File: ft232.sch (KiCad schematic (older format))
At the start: 16 parts, among them J1 USB_B, U6 FT232RL, U7 4N25, U8 4N25

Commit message: Redesigned schematics and board
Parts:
- renumbered C36 to C39, C37 to C40, C38 to C41, D31 to D33, D32 to D34, R45 to R55, R46 to R56, R47 to R57, R48 to R58, R49 to R59, R50 to R60, R51 to R61, U6 to U7, U7 to U8, U8 to U9
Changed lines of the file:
@@
-EESchema Schematic File Version 2  date Thu 19 Jan 2012 12:17:41 AM EST
+EESchema Schematic File Version 2  date Fri 20 Jan 2012 02:23:37 PM EST
 LIBS:power
 LIBS:device
@@
 Sheet 7 7
 Title ""
-Date "19 jan 2012"
+Date "20 jan 2012"
 Rev ""
 Comp ""
@@
 Connection ~ 4250 3650
 $Comp
-L CP1 C37
+L CP1 C40
 U 1 1 4F179530
 P 4000 2000
-F 0 "C37" H 4050 2100 50  0000 L CNN
+F 0 "C40" H 4050 2100 50  0000 L CNN
 F 1 "4.7uF" H 4050 1900 50  0000 L CNN
 	1    4000 2000
@@
 5v-USB
 $Comp
-L R R45
+L R R55
 U 1 1 4F1794BF
 P 4500 3650
-F 0 "R45" V 4580 3650 50  0000 C CNN
+F 0 "R55" V 4580 3650 50  0000 C CNN
 F 1 "2k" V 4500 3650 50  0000 C CNN
 	1    4500 3650
@@
 $EndComp
 $Comp
-L R R51
+L R R61
 U 1 1 4F17944E
 P 10850 3000
-F 0 "R51" V 10930 3000 50  0000 C CNN
+F 0 "R61" V 10930 3000 50  0000 C CNN
 F 1 "2.4k" V 10850 3000 50  0000 C CNN
 	1    10850 3000
@@
 5v-USB
 $Comp
-L R R49
+L R R59
 U 1 1 4F1793A2
 P 9400 3100
-F 0 "R49" V 9480 3100 50  0000 C CNN
+F 0 "R59" V 9480 3100 50  0000 C CNN
 F 1 "10k" V 9400 3100 50  0000 C CNN
 	1    9400 3100
@@
 GND
 $Comp
-L R R50
+L R R60
 U 1 1 4F1792E7
 P 9600 2050
-F 0 "R50" V 9680 2050 50  0000 C CNN
+F 0 "R60" V 9680 2050 50  0000 C CNN
 F 1 "10k" V 9600 2050 50  0000 C CNN
 	1    9600 2050
@@
 NoConn ~ 9350 2200
 $Comp
-L R R46
+L R R56
 U 1 1 4F179239
 P 8100 1950
-F 0 "R46" V 8180 1950 50  0000 C CNN
+F 0 "R56" V 8180 1950 50  0000 C CNN
 F 1 "2.4k" V 8100 1950 50  0000 C CNN
 	1    8100 1950
@@
 5v-USB
 $Comp
-L OPTO-TRANSISTOR U8
+L OPTO-TRANSISTOR U9
 U 1 1 4F1790EA
 P 10200 3450
-F 0 "U8" H 10400 3750 60  0000 C CNN
+F 0 "U9" H 10400 3750 60  0000 C CNN
 F 1 "4N25" H 10300 3150 60  0000 C CNN
 	1    10200 3450
@@
 $EndComp
 $Comp
-L OPTO-TRANSISTOR U7
+L OPTO-TRANSISTOR U8
 U 1 1 4F1790E6
 P 8750 2400
-F 0 "U7" H 8950 2700 60  0000 C CNN
+F 0 "U8" H 8950 2700 60  0000 C CNN
 F 1 "4N25" H 8850 2100 60  0000 C CNN
 	1    8750 2400
@@
 USB-GND
 $Comp
-L C C36
+L C C39
 U 1 1 4F0A45B0
 P 3550 2000
-F 0 "C36" H 3600 2100 50  0000 L CNN
+F 0 "C39" H 3600 2100 50  0000 L CNN
 F 1 "0.1uF" H 3600 1900 50  0000 L CNN
 	1    3550 2000
@@
 NoConn ~ 2200 2650
 $Comp
-L R R48
+L R R58
 U 1 1 4F0A4640
 P 8150 3950
-F 0 "R48" V 8230 3950 50  0000 C CNN
+F 0 "R58" V 8230 3950 50  0000 C CNN
 F 1 "470" V 8150 3950 50  0000 C CNN
 	1    8150 3950
@@
 $EndComp
 $Comp
-L R R47
+L R R57
 U 1 1 4F0A462A
 P 8150 3650
-F 0 "R47" V 8230 3650 50  0000 C CNN
+F 0 "R57" V 8230 3650 50  0000 C CNN
 F 1 "470" V 8150 3650 50  0000 C CNN
 	1    8150 3650
@@
 $EndComp
 $Comp
-L LED D32
+L LED D34
 U 1 1 4F0A4611
 P 7700 3950
-F 0 "D32" H 7700 4050 50  0000 C CNN
+F 0 "D34" H 7700 4050 50  0000 C CNN
 F 1 "LED" H 7700 3850 50  0000 C CNN
 	1    7700 3950
@@
 $EndComp
 $Comp
-L LED D31
+L LED D33
 U 1 1 4F0A45FE
 P 7700 3650
-F 0 "D31" H 7700 3750 50  0000 C CNN
+F 0 "D33" H 7700 3750 50  0000 C CNN
 F 1 "LED" H 7700 3550 50  0000 C CNN
 	1    7700 3650
@@
 $EndComp
 $Comp
-L C C38
+L C C41
 U 1 1 4F0A4530
 P 4950 4350
-F 0 "C38" H 5000 4450 50  0000 L CNN
+F 0 "C41" H 5000 4450 50  0000 L CNN
 F 1 "0.1uF" H 5000 4250 50  0000 L CNN
 	1    4950 4350
@@
 NoConn ~ 6800 4150
 $Comp
-L FT232RL U6
+L FT232RL U7
 U 1 1 4F0A4204
 P 5900 3650
-F 0 "U6" H 6300 2700 60  0000 C CNN
+F 0 "U7" H 6300 2700 60  0000 C CNN
 F 1 "FT232RL" H 5900 4550 60  0000 C CNN
 	1    5900 3650

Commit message: Updated Schematics, created new PDF, completed board layout and routing
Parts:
- removed U8, U9: 4N25, symbol OPTO-TRANSISTOR
- added JP3, JP4: JUMPER, symbol JUMPER
- added U8, U9: PS2911-1-F3-A, symbol PS2911-1-F3-A
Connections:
- wire segments 28 -> 30
- no-connect marks 15 -> 11
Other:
- moved on the sheet: R60, R61
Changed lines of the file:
@@
-EESchema Schematic File Version 2  date Fri 20 Jan 2012 02:23:37 PM EST
+EESchema Schematic File Version 2  date Sun 22 Jan 2012 12:58:37 AM EST
 LIBS:power
 LIBS:device
@@
 Sheet 7 7
 Title ""
-Date "20 jan 2012"
+Date "22 jan 2012"
 Rev ""
 Comp ""
@@
 Comment4 ""
 $EndDescr
+Connection ~ 7250 3250
+Connection ~ 7850 3250
+Wire Wire Line
+	7850 3250 7850 3150
+Wire Wire Line
+	7850 3150 6800 3150
+Connection ~ 6800 3450
+Connection ~ 7400 3450
+Wire Wire Line
+	7400 3450 7400 3350
+Wire Wire Line
+	7400 3350 6800 3350
+Connection ~ 4250 3650
+Connection ~ 4750 3650
+Connection ~ 4950 3650
+Wire Wire Line
+	4750 3650 4950 3650
+Connection ~ 6800 3150
+Connection ~ 6800 3250
+Connection ~ 6800 3350
+Connection ~ 6800 3450
+Wire Wire Line
+	9400 2850 9650 2850
+Wire Wire Line
+	6800 2950 8100 2950
+Wire Wire Line
+	8100 2950 8100 2500
+Connection ~ 8100 1700
+Connection ~ 8100 2500
+Connection ~ 9400 2850
+Connection ~ 9400 3350
+Connection ~ 9600 3350
+Connection ~ 9600 3650
+Wire Wire Line
+	9600 3650 9350 3650
+Connection ~ 8100 2200
+Wire Wire Line
+	8400 3950 8400 3650
+Wire Wire Line
+	2550 3150 2550 1800
+Wire Wire Line
+	6200 4850 4950 4850
+Connection ~ 6800 2950
+Connection ~ 6800 3050
+Connection ~ 8400 3950
+Connection ~ 8400 3650
+Connection ~ 7900 3650
+Connection ~ 7900 3950
+Connection ~ 7500 3950
+Connection ~ 7500 3650
+Connection ~ 6800 3750
+Connection ~ 6800 3850
+Connection ~ 6200 4850
+Connection ~ 6050 4850
+Connection ~ 5900 4850
+Connection ~ 5750 4850
+Connection ~ 4950 4550
+Connection ~ 4950 4150
+Connection ~ 4950 3350
+Connection ~ 4950 3250
+Connection ~ 4950 3000
+Connection ~ 4950 2900
+Connection ~ 2550 3450
+Connection ~ 2550 3350
+Connection ~ 2550 3250
+Connection ~ 2550 3150
+Connection ~ 3550 2200
+Connection ~ 3550 1800
+Wire Wire Line
+	7500 3950 7500 3850
+Wire Wire Line
+	7500 3850 6800 3850
+Wire Wire Line
+	2550 3350 4950 3350
+Connection ~ 5600 4850
+Wire Wire Line
+	2550 4550 4950 4550
+Wire Wire Line
+	4950 3250 2550 3250
+Wire Wire Line
+	7500 3650 7500 3750
+Wire Wire Line
+	7500 3750 6800 3750
+Wire Wire Line
+	2550 4550 2550 3450
+Wire Wire Line
+	4950 4550 4950 4850
+Wire Wire Line
+	2550 1800 4950 1800
+Wire Wire Line
+	4950 1800 4950 3000
+Wire Wire Line
+	8100 1700 7850 1700
+Wire Wire Line
+	6800 3050 8850 3050
+Wire Wire Line
+	8850 3050 8850 3350
+Wire Wire Line
+	8850 3350 9600 3350
+Wire Wire Line
+	4250 3650 4000 3650
+Wire Wire Line
+	3550 2200 4000 2200
+Connection ~ 4000 2200
 Connection ~ 4000 1800
-NoConn ~ 10550 3650
-NoConn ~ 8400 2600
-Connection ~ 4000 2200
-Wire Wire Line
-	3550 2200 4000 2200
-Wire Wire Line
-	4250 3650 4000 3650
-Wire Wire Line
-	6800 3350 6800 3450
-Wire Wire Line
-	9600 3350 8850 3350
-Wire Wire Line
-	8850 3350 8850 3050
-Wire Wire Line
-	8850 3050 6800 3050
-Wire Wire Line
-	8100 1700 7850 1700
-Wire Wire Line
-	4950 3000 4950 1800
-Wire Wire Line
-	4950 1800 2550 1800
-Wire Wire Line
-	4950 4550 4950 4850
-Wire Wire Line
-	2550 3450 2550 4550
-Wire Wire Line
-	6800 3750 7500 3750
-Wire Wire Line
-	7500 3750 7500 3650
-Wire Wire Line
-	4950 3250 2550 3250
-Wire Wire Line
-	2550 4550 4950 4550
-Connection ~ 5600 4850
-Wire Wire Line
-	2550 3350 4950 3350
-Wire Wire Line
-	6800 3850 7500 3850
-Wire Wire Line
-	7500 3850 7500 3950
-Connection ~ 3550 1800
-Connection ~ 3550 2200
-Connection ~ 2550 3150
-Connection ~ 2550 3250
-Connection ~ 2550 3350
-Connection ~ 2550 3450
-Connection ~ 4950 2900
-Connection ~ 4950 3000
-Connection ~ 4950 3250
-Connection ~ 4950 3350
-Connection ~ 4950 4150
-Connection ~ 4950 4550
-Connection ~ 5750 4850
-Connection ~ 5900 4850
-Connection ~ 6050 4850
-Connection ~ 6200 4850
-Connection ~ 6800 3850
-Connection ~ 6800 3750
-Connection ~ 7500 3650
-Connection ~ 7500 3950
-Connection ~ 7900 3950
-Connection ~ 7900 3650
-Connection ~ 8400 3650
-Connection ~ 8400 3950
-Connection ~ 6800 3050
-Connection ~ 6800 2950
-Wire Wire Line
-	4950 4850 6200 4850
-Wire Wire Line
-	2550 1800 2550 3150
-Wire Wire Line
-	8400 3950 8400 3650
-Connection ~ 9600 1800
-Connection ~ 9600 2300
-Wire Wire Line
-	9700 2300 9350 2300
-Connection ~ 8100 2200
-Connection ~ 9350 2300
-Connection ~ 9350 2600
-Wire Wire Line
-	9600 3650 9350 3650
-Connection ~ 9600 3650
-Connection ~ 9600 3350
-Connection ~ 9400 3350
-Connection ~ 9400 2850
-Connection ~ 10850 3550
-Connection ~ 8100 2500
-Connection ~ 8100 1700
-Wire Wire Line
-	8100 2500 8100 2950
-Wire Wire Line
-	8100 2950 6800 2950
-Wire Wire Line
-	9400 2850 9650 2850
-Connection ~ 10850 3250
-Connection ~ 10850 2750
-Wire Wire Line
-	6800 3150 6800 3250
-Connection ~ 6800 3450
-Connection ~ 6800 3350
-Connection ~ 6800 3250
-Connection ~ 6800 3150
-Wire Wire Line
-	4750 3650 4950 3650
-Connection ~ 4950 3650
-Connection ~ 4750 3650
-Connection ~ 4250 3650
+Connection ~ 9350 1700
+Connection ~ 9350 2200
+Connection ~ 9350 2500
+Connection ~ 10850 2850
+Connection ~ 10850 3350
+Connection ~ 10850 3650
+Wire Wire Line
+	6800 3250 7250 3250
+$Comp
+L JUMPER JP4
+U 1 1 4F1B747C
+P 7550 3250
+F 0 "JP4" H 7550 3400 60  0000 C CNN
+F 1 "JUMPER" H 7550 3170 40  0000 C CNN
+	1    7550 3250
+	1    0    0    -1
+$EndComp
+$Comp
+L JUMPER JP3
+U 1 1 4F1B7347
+P 7100 3450
+F 0 "JP3" H 7100 3600 60  0000 C CNN
+F 1 "JUMPER" H 7100 3370 40  0000 C CNN
+	1    7100 3450
+	1    0    0    -1
+$EndComp
+$Comp
+L PS2911-1-F3-A U9
+U 1 1 4F1B4731
+P 10200 3550
+F 0 "U9" H 10400 3850 60  0000 C CNN
+F 1 "PS2911-1-F3-A" H 10150 3350 60  0000 C CNN
+	1    10200 3550
+	-1   0    0    -1
+$EndComp
+$Comp
+L PS2911-1-F3-A U8
+U 1 1 4F1B46FD
+P 8750 2400
+F 0 "U8" H 8950 2700 60  0000 C CNN
+F 1 "PS2911-1-F3-A" H 8700 2200 60  0000 C CNN
+	1    8750 2400
+	1    0    0    -1
+$EndComp
 $Comp
 L CP1 C40
@@
 L R R61
 U 1 1 4F17944E
-P 10850 3000
-F 0 "R61" V 10930 3000 50  0000 C CNN
-F 1 "2.4k" V 10850 3000 50  0000 C CNN
-	1    10850 3000
-	1    0    0    -1
-$EndComp
-Text HLabel 10850 2750 2    40   Input ~ 0
+P 10850 3100
+F 0 "R61" V 10930 3100 50  0000 C CNN
+F 1 "2.4k" V 10850 3100 50  0000 C CNN
+	1    10850 3100
+	1    0    0    -1
+$EndComp
+Text HLabel 10850 2850 2    40   Input ~ 0
 5vdc
-NoConn ~ 9600 3250
 Text Label 9400 2850 0    40   ~ 0
 5v-USB
@@
 Text Label 9600 3650 2    40   ~ 0
 USB-GND
-Text HLabel 9350 2600 2    40   Input ~ 0
+Text HLabel 9350 2500 2    40   Input ~ 0
 GND
 $Comp
 L R R60
 U 1 1 4F1792E7
-P 9600 2050
-F 0 "R60" V 9680 2050 50  0000 C CNN
-F 1 "10k" V 9600 2050 50  0000 C CNN
-	1    9600 2050
-	1    0    0    -1
-$EndComp
-NoConn ~ 9350 2200
+P 9350 1950
+F 0 "R60" V 9430 1950 50  0000 C CNN
+F 1 "10k" V 9350 1950 50  0000 C CNN
+	1    9350 1950
+	1    0    0    -1
+$EndComp
 $Comp
 L R R56
@@
 Text Label 2700 1800 0    40   ~ 0
 5v-USB
-$Comp
-L OPTO-TRANSISTOR U9
-U 1 1 4F1790EA
-P 10200 3450
-F 0 "U9" H 10400 3750 60  0000 C CNN
-F 1 "4N25" H 10300 3150 60  0000 C CNN
-	1    10200 3450
-	-1   0    0    -1
-$EndComp
-$Comp
-L OPTO-TRANSISTOR U8
-U 1 1 4F1790E6
-P 8750 2400
-F 0 "U8" H 8950 2700 60  0000 C CNN
-F 1 "4N25" H 8850 2100 60  0000 C CNN
-	1    8750 2400
-	1    0    0    -1
-$EndComp
 Text Label 3550 2200 2    40   ~ 0
 USB-GND
@@
 NoConn ~ 4950 3950
 NoConn ~ 4950 3850
-Text HLabel 9700 2300 2    40   BiDi ~ 0
+Text HLabel 9350 2200 2    40   BiDi ~ 0
 RX
-Text HLabel 10850 3550 2    40   BiDi ~ 0
+Text HLabel 10850 3650 2    40   BiDi ~ 0
 TX
-Text HLabel 9600 1800 2    40   Input ~ 0
+Text HLabel 9350 1700 2    40   Input ~ 0
 5vdc
 NoConn ~ 6800 3650

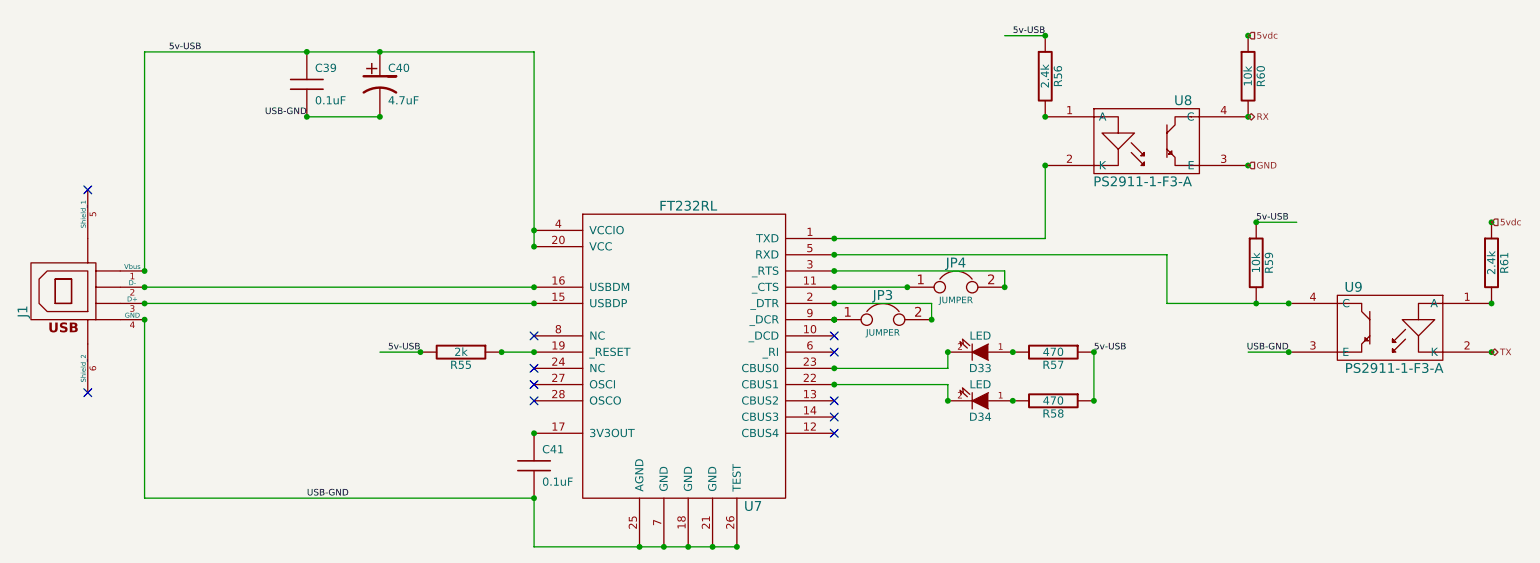
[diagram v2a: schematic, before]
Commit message: Modified: schematics to correct errors
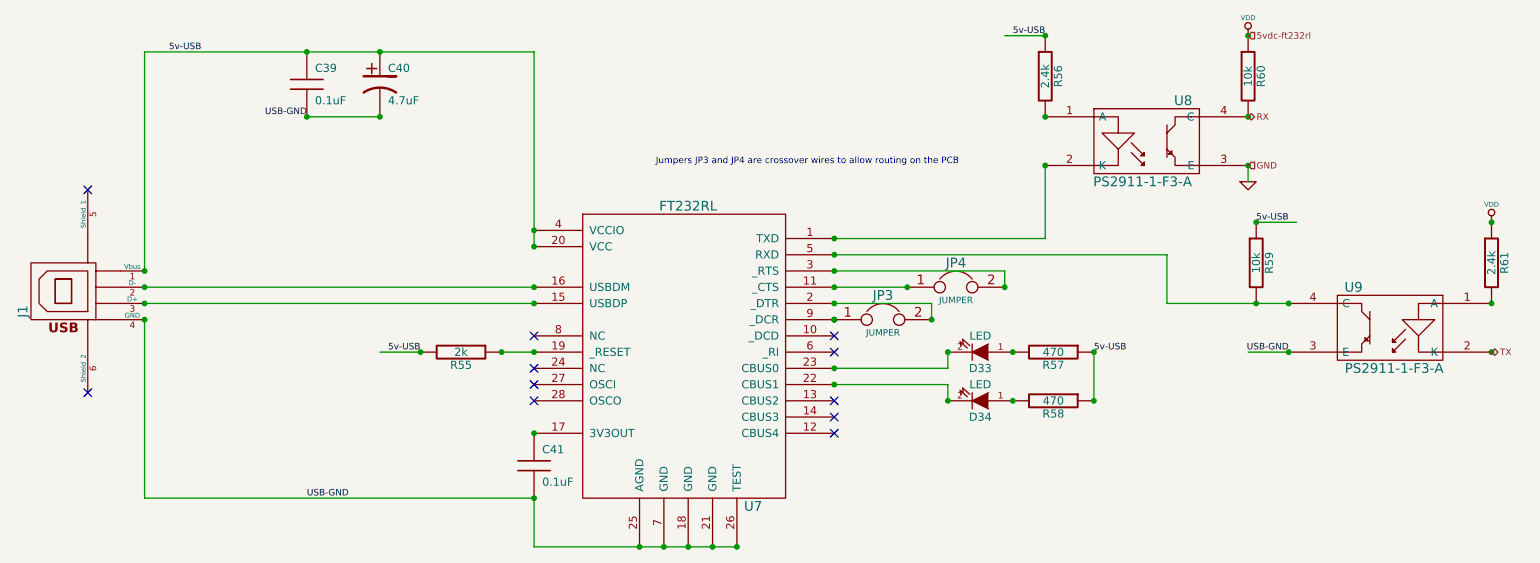
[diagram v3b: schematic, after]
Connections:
- net labels added: 5vdc-ft232rl, VDD
- net labels removed: 5vdc
- wire segments 30 -> 31
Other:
- note added: "Jumpers JP3 and JP4 are crossover wires to allow routing on the PCB"
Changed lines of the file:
@@
-EESchema Schematic File Version 2  date Sun 22 Jan 2012 12:58:37 AM EST
+EESchema Schematic File Version 2  date Sun 22 Jan 2012 05:59:51 PM EST
 LIBS:power
 LIBS:device
@@
 Comment4 ""
 $EndDescr
+$Comp
+L VDD #PWR59
+U 1 1 4F1C4720
+P 10850 2850
+F 0 "#PWR59" H 10850 2950 30  0001 C CNN
+F 1 "VDD" H 10850 2960 30  0000 C CNN
+	1    10850 2850
+	1    0    0    -1
+$EndComp
+$Comp
+L VDD #PWR57
+U 1 1 4F1C4712
+P 9350 1700
+F 0 "#PWR57" H 9350 1800 30  0001 C CNN
+F 1 "VDD" H 9350 1810 30  0000 C CNN
+	1    9350 1700
+	1    0    0    -1
+$EndComp
+Text HLabel 9350 2500 2    40   Input ~ 0
+GND
+Text Notes 5700 2500 0    40   ~ 0
+Jumpers JP3 and JP4 are crossover wires to allow routing on the PCB
+Wire Wire Line
+	9350 2600 9350 2500
+Wire Wire Line
+	6800 3250 7250 3250
+Connection ~ 10850 3650
+Connection ~ 10850 3350
+Connection ~ 10850 2850
+Connection ~ 9350 2500
+Connection ~ 9350 2200
+Connection ~ 9350 1700
+Connection ~ 4000 1800
+Connection ~ 4000 2200
+Wire Wire Line
+	3550 2200 4000 2200
+Wire Wire Line
+	4250 3650 4000 3650
+Wire Wire Line
+	9600 3350 8850 3350
+Wire Wire Line
+	8850 3350 8850 3050
+Wire Wire Line
+	8850 3050 6800 3050
+Wire Wire Line
+	8100 1700 7850 1700
+Wire Wire Line
+	4950 3000 4950 1800
+Wire Wire Line
+	4950 1800 2550 1800
+Wire Wire Line
+	4950 4550 4950 4850
+Wire Wire Line
+	2550 3450 2550 4550
+Wire Wire Line
+	6800 3750 7500 3750
+Wire Wire Line
+	7500 3750 7500 3650
+Wire Wire Line
+	4950 3250 2550 3250
+Wire Wire Line
+	2550 4550 4950 4550
+Connection ~ 5600 4850
+Wire Wire Line
+	2550 3350 4950 3350
+Wire Wire Line
+	6800 3850 7500 3850
+Wire Wire Line
+	7500 3850 7500 3950
+Connection ~ 3550 1800
+Connection ~ 3550 2200
+Connection ~ 2550 3150
+Connection ~ 2550 3250
+Connection ~ 2550 3350
+Connection ~ 2550 3450
+Connection ~ 4950 2900
+Connection ~ 4950 3000
+Connection ~ 4950 3250
+Connection ~ 4950 3350
+Connection ~ 4950 4150
+Connection ~ 4950 4550
+Connection ~ 5750 4850
+Connection ~ 5900 4850
+Connection ~ 6050 4850
+Connection ~ 6200 4850
+Connection ~ 6800 3850
+Connection ~ 6800 3750
+Connection ~ 7500 3650
+Connection ~ 7500 3950
+Connection ~ 7900 3950
+Connection ~ 7900 3650
+Connection ~ 8400 3650
+Connection ~ 8400 3950
+Connection ~ 6800 3050
+Connection ~ 6800 2950
+Wire Wire Line
+	4950 4850 6200 4850
+Wire Wire Line
+	2550 1800 2550 3150
+Wire Wire Line
+	8400 3950 8400 3650
+Connection ~ 8100 2200
+Wire Wire Line
+	9600 3650 9350 3650
+Connection ~ 9600 3650
+Connection ~ 9600 3350
+Connection ~ 9400 3350
+Connection ~ 9400 2850
+Connection ~ 8100 2500
+Connection ~ 8100 1700
+Wire Wire Line
+	8100 2500 8100 2950
+Wire Wire Line
+	8100 2950 6800 2950
+Wire Wire Line
+	9400 2850 9650 2850
+Connection ~ 6800 3450
+Connection ~ 6800 3350
+Connection ~ 6800 3250
+Connection ~ 6800 3150
+Wire Wire Line
+	4750 3650 4950 3650
+Connection ~ 4950 3650
+Connection ~ 4750 3650
+Connection ~ 4250 3650
+Wire Wire Line
+	6800 3350 7400 3350
+Wire Wire Line
+	7400 3350 7400 3450
+Connection ~ 7400 3450
+Connection ~ 6800 3450
+Wire Wire Line
+	6800 3150 7850 3150
+Wire Wire Line
+	7850 3150 7850 3250
+Connection ~ 7850 3250
 Connection ~ 7250 3250
-Connection ~ 7850 3250
-Wire Wire Line
-	7850 3250 7850 3150
-Wire Wire Line
-	7850 3150 6800 3150
-Connection ~ 6800 3450
-Connection ~ 7400 3450
-Wire Wire Line
-	7400 3450 7400 3350
-Wire Wire Line
-	7400 3350 6800 3350
-Connection ~ 4250 3650
-Connection ~ 4750 3650
-Connection ~ 4950 3650
-Wire Wire Line
-	4750 3650 4950 3650
-Connection ~ 6800 3150
-Connection ~ 6800 3250
-Connection ~ 6800 3350
-Connection ~ 6800 3450
-Wire Wire Line
-	9400 2850 9650 2850
-Wire Wire Line
-	6800 2950 8100 2950
-Wire Wire Line
-	8100 2950 8100 2500
-Connection ~ 8100 1700
-Connection ~ 8100 2500
-Connection ~ 9400 2850
-Connection ~ 9400 3350
-Connection ~ 9600 3350
-Connection ~ 9600 3650
-Wire Wire Line
-	9600 3650 9350 3650
-Connection ~ 8100 2200
-Wire Wire Line
-	8400 3950 8400 3650
-Wire Wire Line
-	2550 3150 2550 1800
-Wire Wire Line
-	6200 4850 4950 4850
-Connection ~ 6800 2950
-Connection ~ 6800 3050
-Connection ~ 8400 3950
-Connection ~ 8400 3650
-Connection ~ 7900 3650
-Connection ~ 7900 3950
-Connection ~ 7500 3950
-Connection ~ 7500 3650
-Connection ~ 6800 3750
-Connection ~ 6800 3850
-Connection ~ 6200 4850
-Connection ~ 6050 4850
-Connection ~ 5900 4850
-Connection ~ 5750 4850
-Connection ~ 4950 4550
-Connection ~ 4950 4150
-Connection ~ 4950 3350
-Connection ~ 4950 3250
-Connection ~ 4950 3000
-Connection ~ 4950 2900
-Connection ~ 2550 3450
-Connection ~ 2550 3350
-Connection ~ 2550 3250
-Connection ~ 2550 3150
-Connection ~ 3550 2200
-Connection ~ 3550 1800
-Wire Wire Line
-	7500 3950 7500 3850
-Wire Wire Line
-	7500 3850 6800 3850
-Wire Wire Line
-	2550 3350 4950 3350
-Connection ~ 5600 4850
-Wire Wire Line
-	2550 4550 4950 4550
-Wire Wire Line
-	4950 3250 2550 3250
-Wire Wire Line
-	7500 3650 7500 3750
-Wire Wire Line
-	7500 3750 6800 3750
-Wire Wire Line
-	2550 4550 2550 3450
-Wire Wire Line
-	4950 4550 4950 4850
-Wire Wire Line
-	2550 1800 4950 1800
-Wire Wire Line
-	4950 1800 4950 3000
-Wire Wire Line
-	8100 1700 7850 1700
-Wire Wire Line
-	6800 3050 8850 3050
-Wire Wire Line
-	8850 3050 8850 3350
-Wire Wire Line
-	8850 3350 9600 3350
-Wire Wire Line
-	4250 3650 4000 3650
-Wire Wire Line
-	3550 2200 4000 2200
-Connection ~ 4000 2200
-Connection ~ 4000 1800
-Connection ~ 9350 1700
-Connection ~ 9350 2200
-Connection ~ 9350 2500
-Connection ~ 10850 2850
-Connection ~ 10850 3350
-Connection ~ 10850 3650
-Wire Wire Line
-	6800 3250 7250 3250
+$Comp
+L GND #PWR58
+U 1 1 4F1C30B1
+P 9350 2600
+F 0 "#PWR58" H 9350 2600 30  0001 C CNN
+F 1 "GND" H 9350 2530 30  0001 C CNN
+	1    9350 2600
+	1    0    0    -1
+$EndComp
 $Comp
 L JUMPER JP4
@@
 	1    0    0    -1
 $EndComp
-Text HLabel 10850 2850 2    40   Input ~ 0
-5vdc
 Text Label 9400 2850 0    40   ~ 0
 5v-USB
@@
 Text Label 9600 3650 2    40   ~ 0
 USB-GND
-Text HLabel 9350 2500 2    40   Input ~ 0
-GND
 $Comp
 L R R60
@@
 TX
 Text HLabel 9350 1700 2    40   Input ~ 0
-5vdc
+5vdc-ft232rl
 NoConn ~ 6800 3650
 NoConn ~ 6800 3550
